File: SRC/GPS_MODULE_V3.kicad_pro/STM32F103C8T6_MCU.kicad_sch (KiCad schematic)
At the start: 29 parts, among them J5 Conn_02x03_Odd_Even, U2 STM32F103C8Tx, Y1 8MHz, Y2 32.678KHz

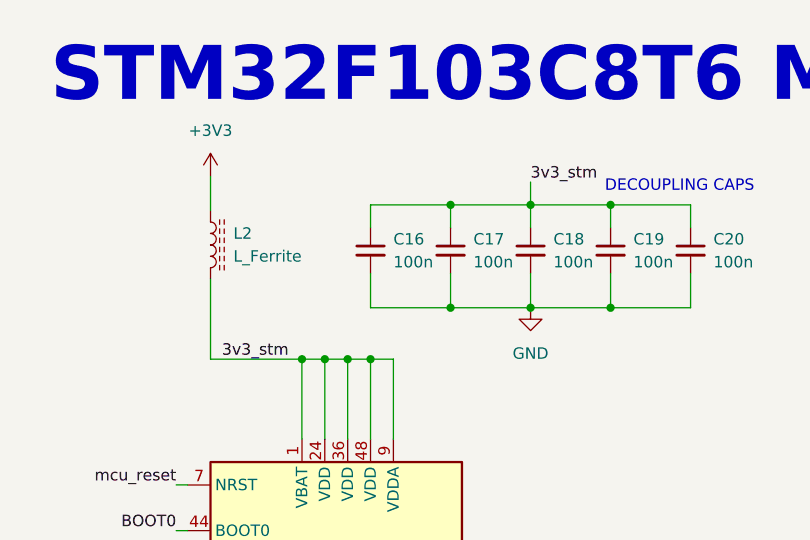
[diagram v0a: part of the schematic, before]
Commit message: gps update on buck 3v3
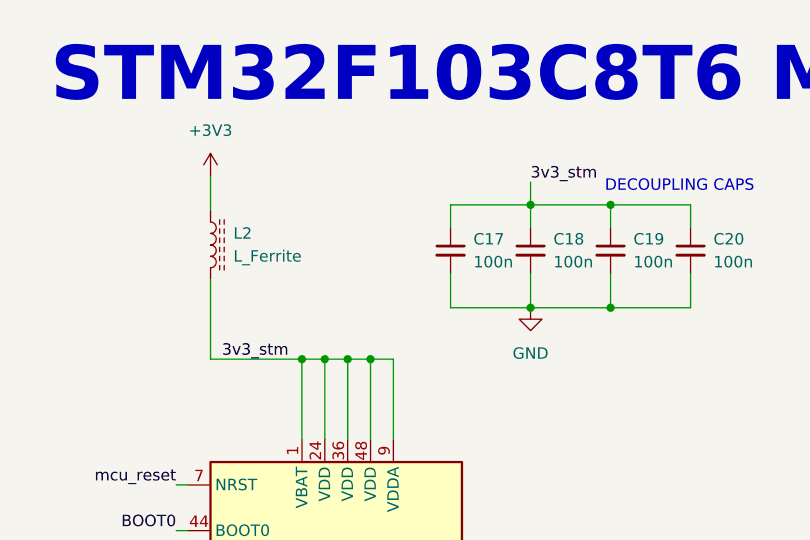
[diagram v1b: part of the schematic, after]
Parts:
- removed C16: 100n, Capacitor_SMD:C_0402_1005Metric, symbol Device:C_Small
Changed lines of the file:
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@@
   (junction (at 191.135 116.205) (diameter 0) (color 0 0 0 0)
   )
-  (junction (at 160.655 34.29) (diameter 0) (color 0 0 0 0)
-  )
   (junction (at 146.685 51.435) (diameter 0) (color 0 0 0 0)
   )
@@
   )
   (junction (at 144.145 51.435) (diameter 0) (color 0 0 0 0)
-  )
-  (junction (at 160.655 45.72) (diameter 0) (color 0 0 0 0)
   )
   (junction (at 146.685 139.065) (diameter 0) (color 0 0 0 0)
@@
     (stroke (width 0) (type default))
   )
-  (wire (pts (xy 151.765 34.29) (xy 151.765 36.83))
-    (stroke (width 0) (type default))
-  )
   (wire (pts (xy 164.465 123.825) (xy 177.165 123.825))
     (stroke (width 0) (type default))
@@
     (stroke (width 0) (type default))
   )
-  (wire (pts (xy 160.655 34.29) (xy 151.765 34.29))
-    (stroke (width 0) (type default))
-  )
   (wire (pts (xy 108.0919 131.3658) (xy 108.0919 131.445))
     (stroke (width 0) (type default))
@@
     (stroke (width 0) (type default))
   )
-  (wire (pts (xy 151.765 41.91) (xy 151.765 45.72))
-    (stroke (width 0) (type default))
-  )
   (polyline (pts (xy 30.48 23.495) (xy 96.52 23.495))
     (stroke (width 0) (type default))
@@
   )
   (wire (pts (xy 229.87 85.725) (xy 229.87 86.995))
-    (stroke (width 0) (type default))
-  )
-  (wire (pts (xy 151.765 45.72) (xy 160.655 45.72))
     (stroke (width 0) (type default))
   )
@@
         )
       )
-    )
-  )
-  (symbol (lib_id "Device:C_Small") (at 151.765 39.37 0) (unit 1)
-    (in_bom yes) (on_board yes) (dnp no) (fields_autoplaced)
-    (property "Reference" "C16" (at 154.305 38.1062 0)
-      (effects (font (size 1.27 1.27)) (justify left))
-    )
-    (property "Value" "100n" (at 154.305 40.6462 0)
-      (effects (font (size 1.27 1.27)) (justify left))
-    )
-    (property "Footprint" "Capacitor_SMD:C_0402_1005Metric" (at 151.765 39.37 0)
-      (effects (font (size 1.27 1.27)) hide)
-    )
-    (property "Datasheet" "~" (at 151.765 39.37 0)
-      (effects (font (size 1.27 1.27)) hide)
-    )
-    (pin "1")
-    (pin "2")
-    (instances
-      (project "ALERT_RIDER_HARDWARE"
-        (path "/6bd12930-91c7-432a-9f98-f9ae5061d3a7/d867153f-866e-4815-8450-e9b125a4b7ea"
-          (reference "C16") (unit 1)
-        )
-      )
-      (project "GPS_MODULE_V3.kicad_pro"
-        (path "/8cb1db64-3fcc-4fb6-aa5a-7b4a50bb28df/8c15b503-edc1-48ce-9a71-ab9546bdf0c8"
-          (reference "C11") (unit 1)
-        )
-      )
-      (project "BIM_PCB"
-        (path "/b79ebed7-e146-448b-8dab-0aefb3e182ca/f23c600c-7725-4edd-91d3-0267a41a1c43"
-          (reference "C1") (unit 1)
-        )
-      )

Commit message: updates on BOM, CPL and gerbers
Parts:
- removed J5: Conn_02x03_Odd_Even, Connector_Molex:Molex_Nano-Fit_105314-xx06_2x03_P2.50mm_Horizontal, symbol Connector_Generic:Conn_02x03_Odd_Even
- removed TP6: Sim_RX, TestPoint:TestPoint_Pad_D1.0mm, symbol Connector:TestPoint
- removed TP7: Sim_TX, TestPoint:TestPoint_Pad_D1.0mm, symbol Connector:TestPoint

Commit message: completed GPS ecoboda files
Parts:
- D5: footprint LED_SMD:LED_0603_1608Metric -> LED_SMD:LED_0402_1005Metric
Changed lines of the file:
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@@
       (effects (font (size 1.27 1.27)) (justify right))
     )
-    (property "Footprint" "LED_SMD:LED_0603_1608Metric" (at 86.36 104.775 0)
+    (property "Footprint" "LED_SMD:LED_0402_1005Metric" (at 86.36 104.775 0)
       (effects (font (size 1.27 1.27)) hide)
     )

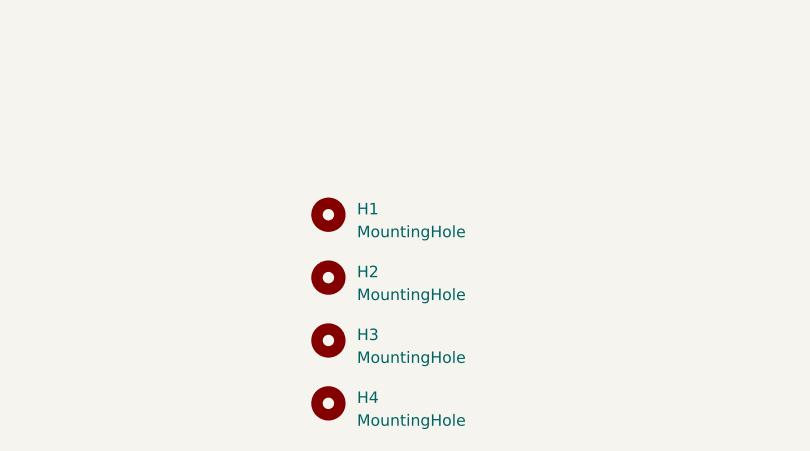
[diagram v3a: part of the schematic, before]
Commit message: update removal of all level shifts diodes
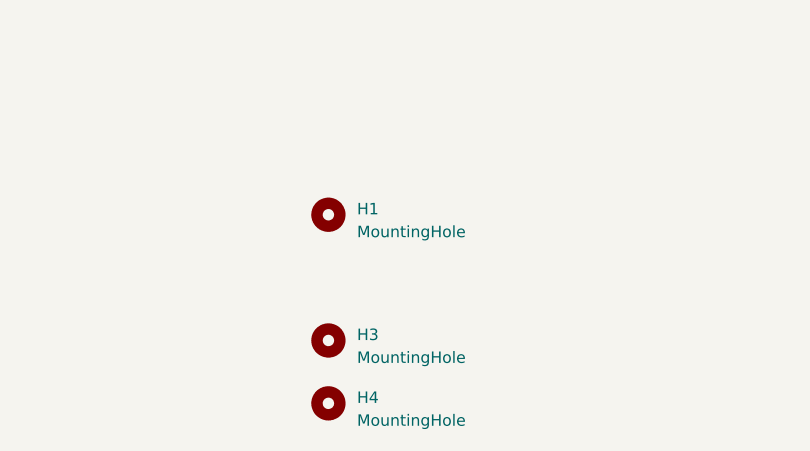
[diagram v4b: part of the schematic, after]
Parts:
- removed H2: MountingHole, MountingHole:MountingHole_2.7mm, symbol Mechanical:MountingHole
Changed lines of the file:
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@@
-    )
-  )
-  (symbol (lib_id "Mechanical:MountingHole") (at 135.255 178.435 0) (unit 1)
-    (in_bom yes) (on_board yes) (dnp no) (fields_autoplaced)
-    (property "Reference" "H2" (at 138.43 177.8 0)
-      (effects (font (size 1.27 1.27)) (justify left))
-    )
-    (property "Value" "MountingHole" (at 138.43 180.34 0)
-      (effects (font (size 1.27 1.27)) (justify left))
-    )
-    (property "Footprint" "MountingHole:MountingHole_2.7mm" (at 135.255 178.435 0)
-      (effects (font (size 1.27 1.27)) hide)
-    )
-    (property "Datasheet" "~" (at 135.255 178.435 0)
-      (effects (font (size 1.27 1.27)) hide)
-    )
-    (instances
-      (project "GPS_MODULE_V3.kicad_pro"
-        (path "/8cb1db64-3fcc-4fb6-aa5a-7b4a50bb28df/8c15b503-edc1-48ce-9a71-ab9546bdf0c8"
-          (reference "H2") (unit 1)
-        )
-      )
-      (project "BIM_PCB"
-        (path "/b79ebed7-e146-448b-8dab-0aefb3e182ca/f23c600c-7725-4edd-91d3-0267a41a1c43"
-          (reference "H2") (unit 1)
-        )
-      )
     )
   )

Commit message: GPS all files BOM and placemnt guide files added
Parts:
- L2: footprint Inductor_SMD:L_0603_1608Metric -> Inductor_SMD:L_0402_1005Metric
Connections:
- net RS485_DI: now also U2.21 (PB10); no longer U2.22 (PB11)
- net RS485_RO: now also U2.22 (PB11); no longer U2.21 (PB10)
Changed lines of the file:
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@@
     (effects (font (size 1.27 1.27)) (justify left))
   )
-  (hierarchical_label "RS485_RO" (shape output) (at 108.585 118.745 180) (fields_autoplaced)
+  (hierarchical_label "RS485_RO" (shape output) (at 108.585 121.285 180) (fields_autoplaced)
     (effects (font (size 1.27 1.27) bold) (justify right))
   )
@@
     (effects (font (size 1.27 1.27)) (justify right))
   )
-  (hierarchical_label "RS485_DI" (shape input) (at 108.585 121.285 180) (fields_autoplaced)
+  (hierarchical_label "RS485_DI" (shape input) (at 108.585 118.745 180) (fields_autoplaced)
     (effects (font (size 1.27 1.27) bold) (justify right))
   )
@@
       (effects (font (size 1.27 1.27)) (justify left))
     )
-    (property "Footprint" "Inductor_SMD:L_0603_1608Metric" (at 133.985 38.735 0)
-      (effects (font (size 1.27 1.27)) hide)
-    )
+    (property "Footprint" "Inductor_SMD:L_0402_1005Metric" (at 133.985 38.735 0)
+      (effects (font (size 1.27 1.27)) hide)
+    )
